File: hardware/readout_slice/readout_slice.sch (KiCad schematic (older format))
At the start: 4 parts

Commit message: auto push run at Fri Feb 26 15:29:40 EST 2021
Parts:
- added D?: GREEN, symbol Device:LED
- added J?: Digilent JTAG header, symbol Connector_Generic:Conn_02x07_Odd_Even
- added R?: 100, symbol Device:R
- added TP?: 1.2V_monitor, symbol Connector:TestPoint_2Pole
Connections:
- net labels added: +3V3, +5V, GNDD, JTAG_TCK, JTAG_TDI, JTAG_TDO, JTAG_TMS, PWR_EN, USB_CPEN, USB_D_N, USB_D_P, USB_ID, USB_VBUS
- wire segments 0 -> 95
- no-connect marks 0 -> 3
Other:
- note added: "- \n | Diligent JTAG plug here?\n | g-2 adc board for refrence\n |\n-"
- note added: "-\nTo USB conn? |\n|\n|\n-"
- note added: "?"
- note added: "PWR_GOOD"
- note added: "VCC_MOD"
- note added: "caps?"
- note added: "from FPGA?"
- note added: "one column is gnd\n"

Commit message: auto push run at Sat Feb 27 19:08:26 EST 2021
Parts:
- added J?: RJ45, symbol Connector:RJ45
- added J?: SD_Card, symbol Connector:SD_Card
- added R?: 20k, symbol Device:R
- added SW? (x2): SW_Push_SPDT, symbol Switch:SW_Push_SPDT
- added SW?: SW_SPST, symbol Switch:SW_SPST
- J? (x2): value SODIMM-200 -> Mars ZX2
- J?: footprint (none) -> readout_slice:87832-1420
- TP?: footprint (none) -> TestPoint:TestPoint_2Pads_Pitch5.08mm_Drill1.3mm
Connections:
- net labels added: ETH_A_N, ETH_A_P, ETH_B_N, ETH_B_P, ETH_CTREF, ETH_C_N, ETH_C_P, ETH_D_N, ETH_D_P, ETH_LED_1, ETH_LED_2, IO_MIO40_B13_L16_W10, IO_MIO41_B13_L16_W9, IO_MIO42_B13_L18_W11, IO_MIO43_B13_L18_Y11, IO_MIO44_B13_L14_Y19, IO_MIO45_B13_L14_Y8, PS_POR, PS_SRST, VCC_CFG_MIO_B13
- wire segments 95 -> 154
- no-connect marks 3 -> 5
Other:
- note added: "- Also to USB conn?"
- note added: "-\nMIO 40-45 to SD Card |\n|\n|\n|\n\n|\n-"
- note added: "Hmmmm?"
- note added: "MIo 1-6, 8 for QSPI flash??\n"
- note added: "sheet for external connectivity???\n"
- note removed: "- \n | Diligent JTAG plug here?\n | g-2 adc board for refrence\n |\n-"
- note removed: "from FPGA?"
- note removed: "one column is gnd\n"
- moved on the sheet: D?, J?, R?, TP?

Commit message: auto push run at Tue Mar  9 10:08:09 EST 2021
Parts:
- removed D?: GREEN, symbol Device:LED
- removed J? (x2): Mars ZX2, symbol Connector:SODIMM-200
- removed J?: RJ45, symbol Connector:RJ45
- removed J?: Digilent JTAG header, readout_slice:87832-1420, symbol Connector_Generic:Conn_02x07_Odd_Even
- removed J?: SD_Card, symbol Connector:SD_Card
- removed R?: 100, symbol Device:R
- removed R?: 20k, symbol Device:R
- removed SW? (x2): SW_Push_SPDT, symbol Switch:SW_Push_SPDT
- removed SW?: SW_SPST, symbol Switch:SW_SPST
- removed TP?: 1.2V_monitor, TestPoint:TestPoint_2Pads_Pitch5.08mm_Drill1.3mm, symbol Connector:TestPoint_2Pole
- removed U?: CITIROC1A, Package_QFP:LQFP-160_24x24mm_P0.5mm, symbol readout:CITIROC1A
- added U?: CITIROC1A, Package_QFP:LQFP-160_24x24mm_P0.5mm, symbol readout_slice-rescue:CITIROC1A-readout
- added U? (x2): Mars_ZX2, symbol readout:Mars_ZX2
- U?: symbol readout:CITIROC1A -> readout_slice-rescue:CITIROC1A-readout
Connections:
- net labels removed: +3V3, +5V, ETH_A_N, ETH_A_P, ETH_B_N, ETH_B_P, ETH_CTREF, ETH_C_N, ETH_C_P, ETH_D_N, ETH_D_P, ETH_LED_1, ETH_LED_2, GNDD, IO_MIO40_B13_L16_W10, IO_MIO41_B13_L16_W9, IO_MIO42_B13_L18_W11, IO_MIO43_B13_L18_Y11, IO_MIO44_B13_L14_Y19, IO_MIO45_B13_L14_Y8, JTAG_TCK, JTAG_TDI, JTAG_TDO, JTAG_TMS, PS_POR, PS_SRST, PWR_EN, USB_CPEN, USB_D_N, USB_D_P, USB_ID, USB_VBUS, VCC_CFG_MIO_B13
- wire segments 154 -> 0
- no-connect marks 5 -> 0
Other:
- note removed: "- Also to USB conn?"
- note removed: "-\nMIO 40-45 to SD Card |\n|\n|\n|\n\n|\n-"
- note removed: "-\nTo USB conn? |\n|\n|\n-"
- note removed: "?"
- note removed: "Hmmmm?"
- note removed: "MIo 1-6, 8 for QSPI flash??\n"
- note removed: "PWR_GOOD"
- note removed: "VCC_MOD"
- note removed: "caps?"
- note removed: "sheet for external connectivity???\n"

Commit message: artix7 schematic finished
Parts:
- added U? (x2): XC7A35T-1FGG484, symbol readout:XC7A35T-1FGG484
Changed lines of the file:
@@
 $Descr A 11000 8500
 encoding utf-8
-Sheet 1 3
+Sheet 1 4
 Title "readout_slice"
 Date "2021-02-24"
@@
 S 4600 7050 1250 450
 U 603D0C5A
-F0 "Sheet_power" 50
+F0 "power" 50
 F1 "power.sch" 50
 $EndSheet
@@
 U 608B2FC0
 F0 "connectivity" 50
-F1 "Sheet_connectivity.sch" 50
+F1 "connectivity.sch" 50
 $EndSheet
 $Comp
@@
 	1    0    0    -1
 $EndComp
+$Sheet
+S 3150 6400 1000 500
+U 605605C8
+F0 "FPGA" 50
+F1 "FPGA.sch" 50
+$EndSheet
+$Comp
+L readout:XC7A35T-1FGG484 U?
+U 1 1 6047B697
+P -2550 2700
+F 0 "U?" H -2700 2981 50  0000 C CNN
+F 1 "XC7A35T-1FGG484" H -2700 2890 50  0000 C CNN
+F 2 "" H -3650 2850 50  0001 C CNN
+F 3 "" H -3650 2850 50  0001 C CNN
+	1    -2550 2700
+	1    0    0    -1
+$EndComp
+$Comp
+L readout:XC7A35T-1FGG484 U?
+U 2 1 6047B957
+P -2900 -200
+F 0 "U?" H -3737 -1129 50  0000 R CNN
+F 1 "XC7A35T-1FGG484" H -3737 -1220 50  0000 R CNN
+F 2 "" H -4000 -50 50  0001 C CNN
+F 3 "" H -4000 -50 50  0001 C CNN
+	2    -2900 -200
+	1    0    0    -1
+$EndComp

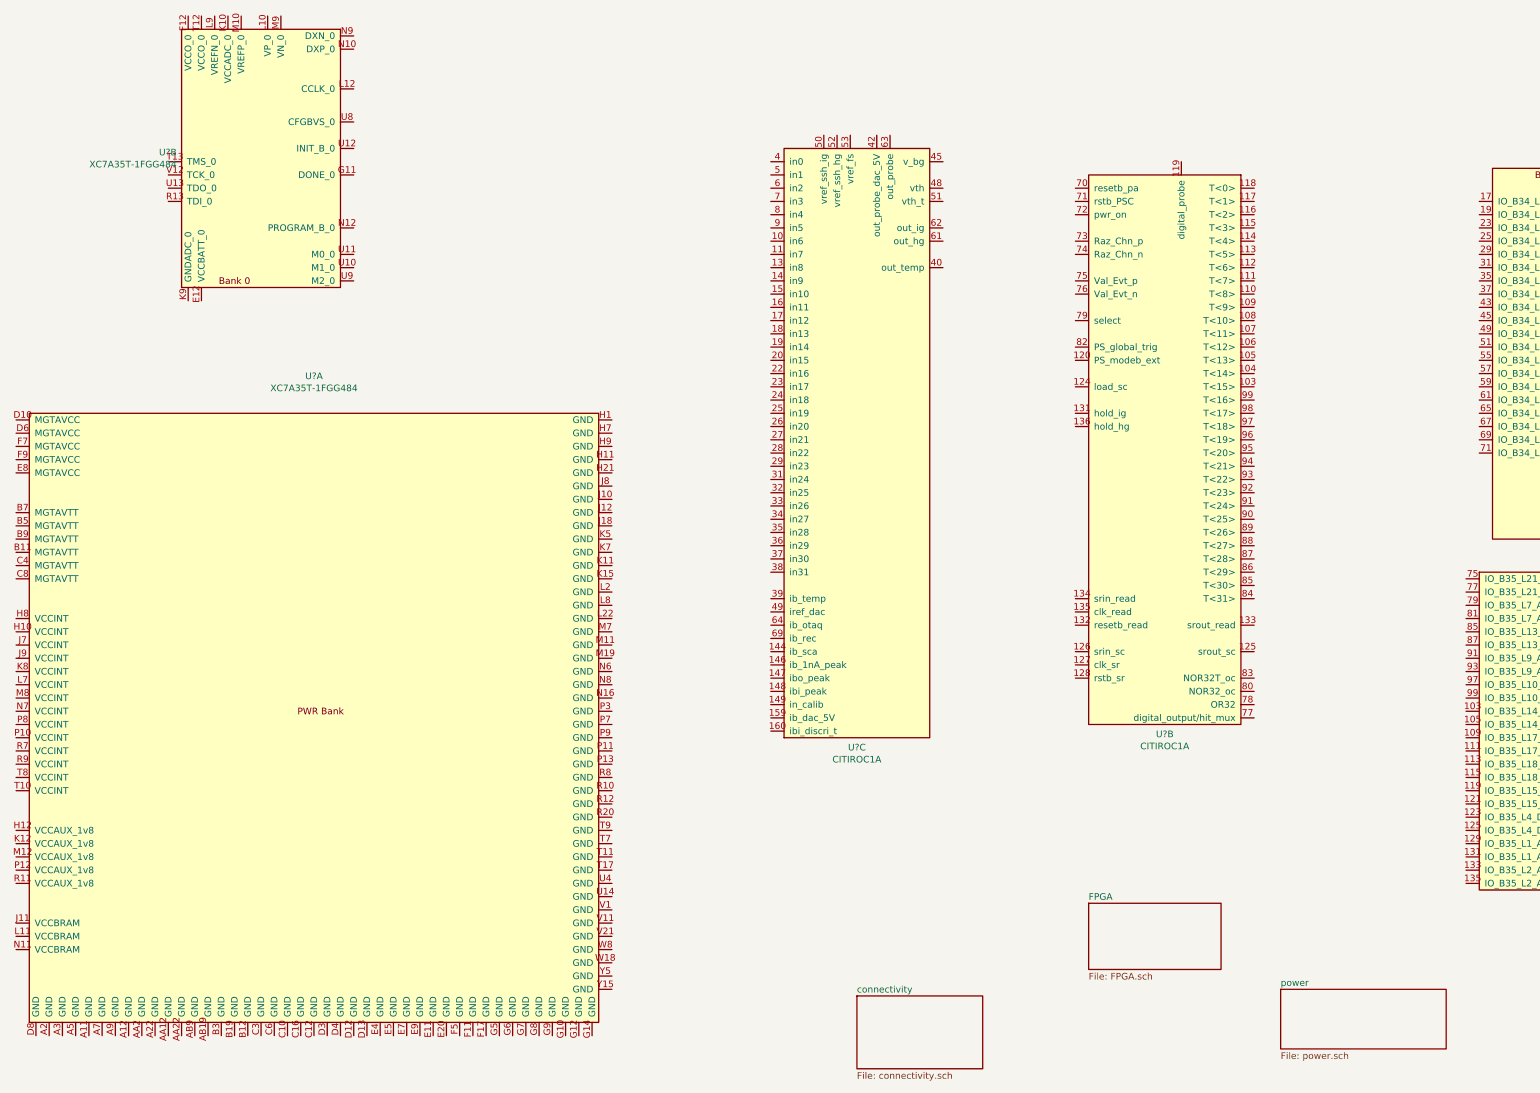
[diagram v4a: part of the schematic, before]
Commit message: more work on moving FPGA components around
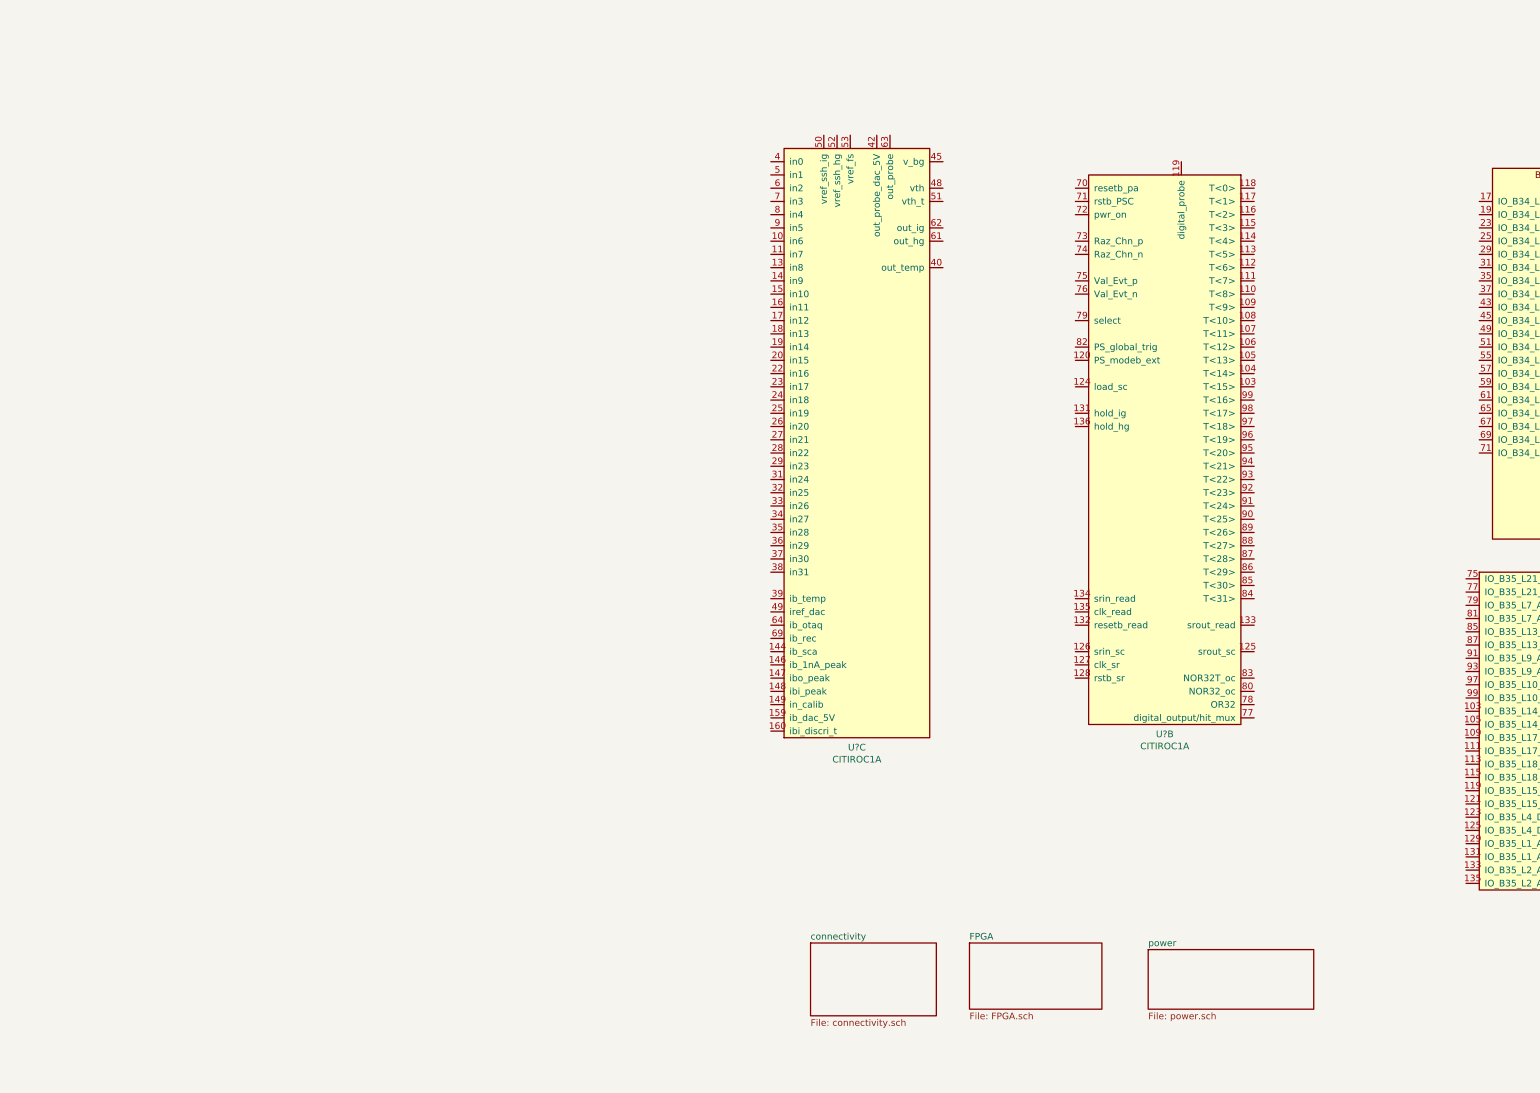
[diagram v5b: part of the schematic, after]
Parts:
- removed U? (x2): XC7A35T-1FGG484, symbol readout:XC7A35T-1FGG484
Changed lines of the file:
@@
 $EndComp
 $Sheet
-S 4600 7050 1250 450
+S 3600 6750 1250 450
 U 603D0C5A
 F0 "power" 50
@@
 $EndComp
 $Sheet
-S 1400 7100 950  550
+S 1050 6700 950  550
 U 608B2FC0
 F0 "connectivity" 50
@@
 $EndComp
 $Sheet
-S 3150 6400 1000 500
+S 2250 6700 1000 500
 U 605605C8
 F0 "FPGA" 50
 F1 "FPGA.sch" 50
 $EndSheet
-$Comp
-L readout:XC7A35T-1FGG484 U?
-U 1 1 6047B697
-P -2550 2700
-F 0 "U?" H -2700 2981 50  0000 C CNN
-F 1 "XC7A35T-1FGG484" H -2700 2890 50  0000 C CNN
-F 2 "" H -3650 2850 50  0001 C CNN
-F 3 "" H -3650 2850 50  0001 C CNN
-	1    -2550 2700
-	1    0    0    -1
-$EndComp
-$Comp
-L readout:XC7A35T-1FGG484 U?
-U 2 1 6047B957
-P -2900 -200
-F 0 "U?" H -3737 -1129 50  0000 R CNN
-F 1 "XC7A35T-1FGG484" H -3737 -1220 50  0000 R CNN
-F 2 "" H -4000 -50 50  0001 C CNN
-F 3 "" H -4000 -50 50  0001 C CNN
-	2    -2900 -200
-	1    0    0    -1
-$EndComp
 $EndSCHEMATC

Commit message: working on readount_slice
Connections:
- net SD_io_CD#: now reaches U?.67 (IO_B34_L17_Y19_N)
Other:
- note added: "make this global"
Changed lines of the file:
@@
 F1 "FPGA.sch" 50
 $EndSheet
+Wire Wire Line
+	6100 2800 5300 2800
+Text Notes 5000 2750 0    50   ~ 10
+make this global
+Text Label 5300 2800 0    50   ~ 10
+SD_io_CD#
 $EndSCHEMATC

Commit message: more work on readout_slice
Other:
- note added: "goes global"
- note removed: "make this global"
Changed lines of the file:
@@
 $EndComp
 $Sheet
-S 3600 6750 1250 450
+S 2750 7050 1250 450
 U 603D0C5A
 F0 "power" 50
 F1 "power.sch" 50
+F2 "PS_SRST" I L 2750 7400 50
 $EndSheet
 $Comp
@@
 $EndComp
 $Sheet
-S 1050 6700 950  550
+S 850  7150 950  550
 U 608B2FC0
 F0 "connectivity" 50
 F1 "connectivity.sch" 50
+F2 "PS_SRST" I R 1800 7650 50
+F3 "SD_id_CD#" I R 1800 7550 50
 $EndSheet
 $Comp
@@
 $EndComp
 $Sheet
-S 2250 6700 1000 500
+S 1850 6100 1000 500
 U 605605C8
 F0 "FPGA" 50
@@
 	6100 2800 5300 2800
 Text Notes 5000 2750 0    50   ~ 10
-make this global
+goes global
 Text Label 5300 2800 0    50   ~ 10
 SD_io_CD#

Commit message: working more on readout_slice schematic
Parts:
- U? (x2): value Mars_ZX2 -> CITIROC1A; footprint (none) -> Package_QFP:LQFP-160_24x24mm_P0.5mm
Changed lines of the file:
@@
 F1 "power.sch" 50
 F2 "PS_SRST" I L 2750 7400 50
+F3 "+3V3" I R 4000 7100 50
+F4 "+5V" I R 4000 7200 50
+F5 "GNDA" I R 4000 7300 50
+F6 "GNDD" I R 4000 7400 50
 $EndSheet
 $Comp
@@
 P 7300 850
 F 0 "U?" H 7275 1025 50  0000 C CNN
-F 1 "Mars_ZX2" H 7275 934 50  0000 C CNN
-F 2 "" H 7350 1200 50  0001 C CNN
-F 3 "" H 7350 1200 50  0001 C CNN
+F 1 "CITIROC1A" H 7275 934 50  0000 C CNN
+F 2 "Package_QFP:LQFP-160_24x24mm_P0.5mm" H 7350 1200 50  0001 C CNN
+F 3 "http://gauss.bu.edu/svn/emphatic-doco/Docs/CITIROC1A%20-%20Datasheet%20V2.5.pdf" H 7350 1200 50  0001 C CNN
 	4    7300 850
 	1    0    0    -1
@@
 P 7200 3900
 F 0 "U?" H 7250 4075 50  0000 C CNN
-F 1 "Mars_ZX2" H 7250 3984 50  0000 C CNN
-F 2 "" H 7250 4250 50  0001 C CNN
-F 3 "" H 7250 4250 50  0001 C CNN
+F 1 "CITIROC1A" H 7250 3984 50  0000 C CNN
+F 2 "Package_QFP:LQFP-160_24x24mm_P0.5mm" H 7250 4250 50  0001 C CNN
+F 3 "http://gauss.bu.edu/svn/emphatic-doco/Docs/CITIROC1A%20-%20Datasheet%20V2.5.pdf" H 7250 4250 50  0001 C CNN
 	5    7200 3900
 	1    0    0    -1
@@
 F2 "PS_SRST" I R 1800 7650 50
 F3 "SD_id_CD#" I R 1800 7550 50
+F4 "Vcc_0" I R 1800 7450 50
 $EndSheet
 $Comp
@@
 F0 "FPGA" 50
 F1 "FPGA.sch" 50
+F2 "Vcc_0" I R 2850 6450 50
 $EndSheet
 Wire Wire Line
